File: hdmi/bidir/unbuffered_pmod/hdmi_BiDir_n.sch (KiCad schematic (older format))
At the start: 32 parts

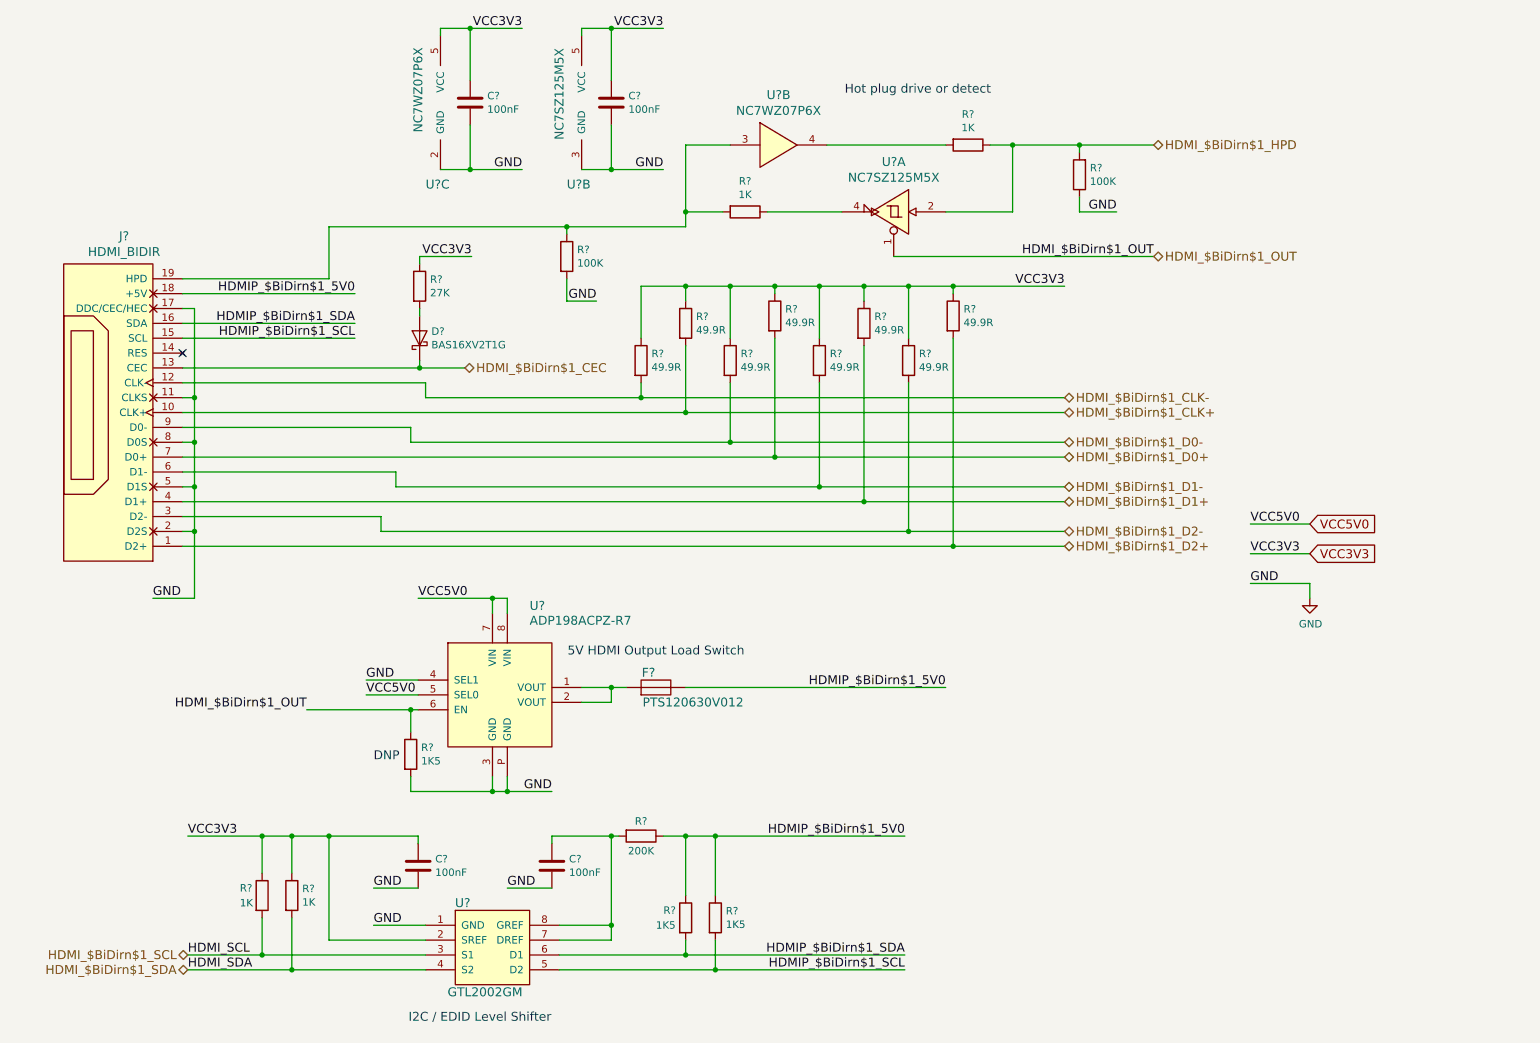
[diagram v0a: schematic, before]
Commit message: Add PMOD Conector and DC/DC Converter
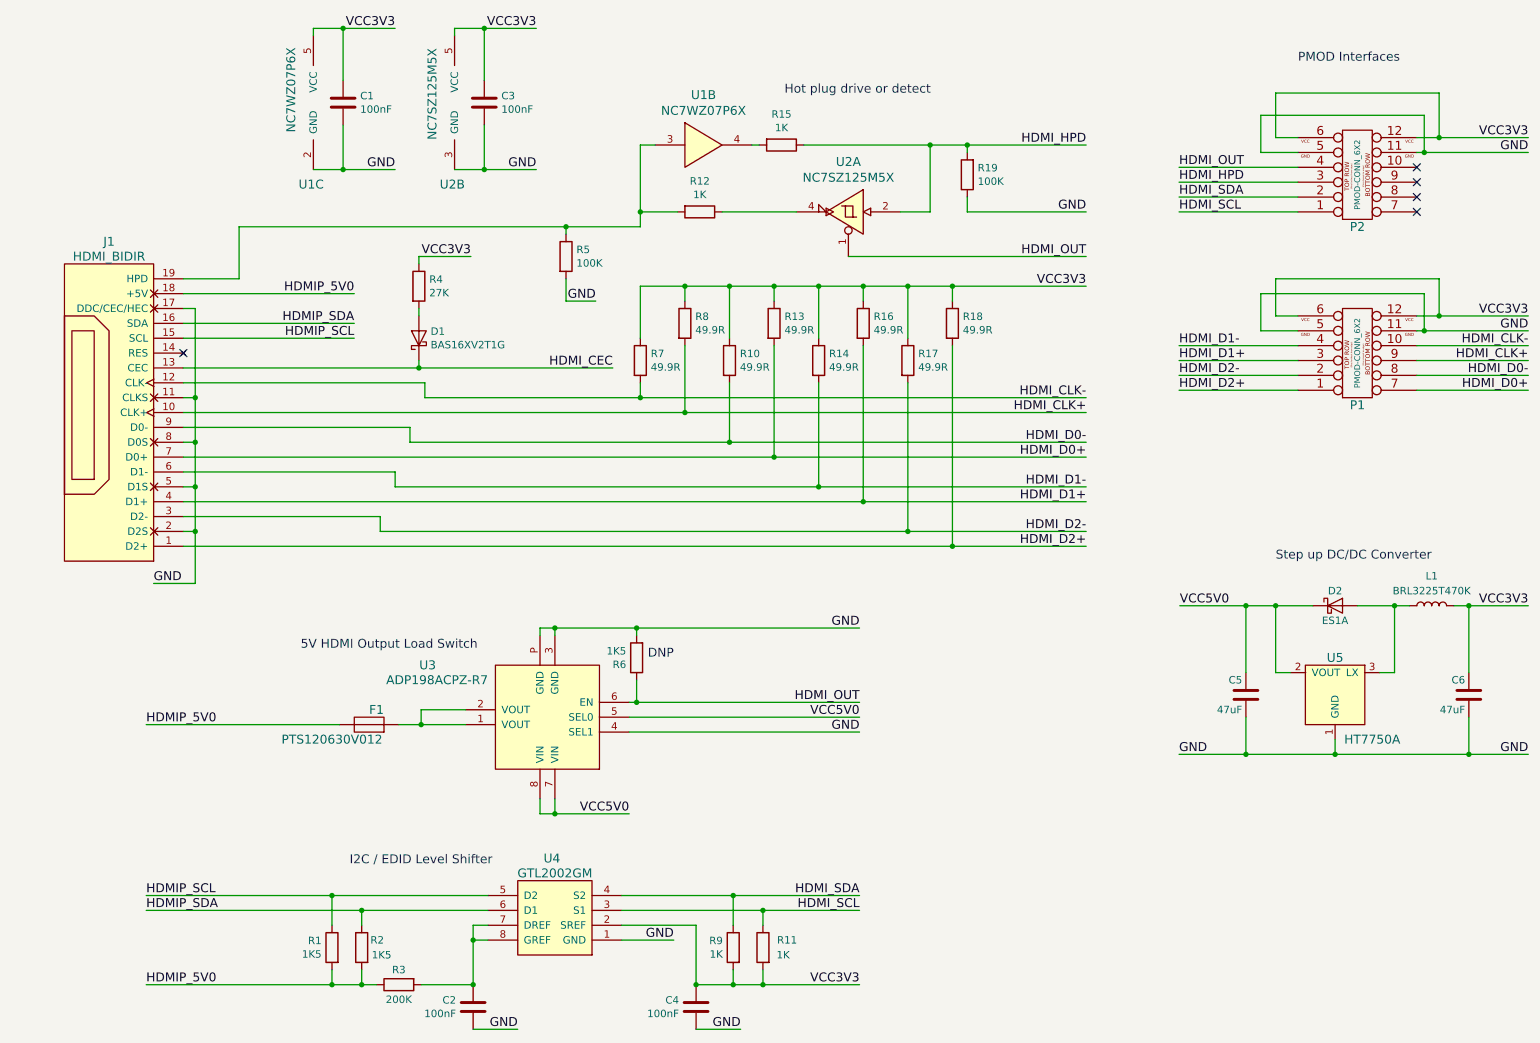
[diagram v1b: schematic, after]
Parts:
- added C5, C6: 47uF, symbol C
- added D2: ES1A, Diodes_SMD:D_SMA_Standard, symbol D_Schottky
- added L1: BRL3225T470K, SMD_Packages:SMD-1210_Pol, symbol L
- added P1, P2: PMOD-CONN_6X2, pmod_pin_array_6x2:pmod_pin_array_6x2, symbol PMOD-CONN_6X2
- added U5: HT7750A, TO_SOT_Packages_SMD:SOT-23, symbol HT7750A
- D1: renamed from D?; footprint (none) -> Diodes_SMD:D_SOD-523
- F1: renamed from F?; footprint (none) -> SMD_Packages:SMD-1206_Pol
- J1: renamed from J?; footprint (none) -> hdmi:HDMI_TH
- U1: renamed from U?; footprint (none) -> TO_SOT_Packages_SMD:SOT-363_SC-70-6
- U2: renamed from U?; footprint (none) -> TO_SOT_Packages_SMD:SOT-23-5
- gave numbers to parts that had none: 25
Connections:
- net GND: now also C5.2, C6.2, P1.11 (P11), P1.5 (P5), P2.11 (P11), P2.5 (P5), U5.1 (GND)
- net VCC3V3: now also R11.2, R9.2, C6.1, L1.2, P1.12 (P12), P1.6 (P6), P2.12 (P12), P2.6 (P6); no longer R11.1, R9.1
- net VCC5V0: now also C5.1, D2.1 (K), U5.2 (VOUT)
- net HDMIP_$BiDirn$1_5V0 renamed HDMIP_5V0
- net HDMIP_5V0: now also R1.2, R2.2; no longer R1.1, R2.1
- net HDMIP_$BiDirn$1_SCL renamed HDMIP_SCL
- net HDMIP_SCL: now also R1.1; no longer R1.2
- net HDMIP_$BiDirn$1_SDA renamed HDMIP_SDA
- net HDMIP_SDA: now also R2.1; no longer R2.2
- net HDMI_$BiDirn$1_CEC renamed HDMI_CEC
- net HDMI_$BiDirn$1_CLK+ renamed HDMI_CLK+
- net HDMI_CLK+: now also P1.9 (P9)
- net HDMI_$BiDirn$1_CLK- renamed HDMI_CLK-
- net HDMI_CLK-: now also P1.10 (P10)
- net HDMI_$BiDirn$1_D0+ renamed HDMI_D0+
- net HDMI_D0+: now also P1.7 (P7)
- net HDMI_$BiDirn$1_D0- renamed HDMI_D0-
- net HDMI_D0-: now also P1.8 (P8)
- net HDMI_$BiDirn$1_D1+ renamed HDMI_D1+
- net HDMI_D1+: now also P1.3 (P3)
- net HDMI_$BiDirn$1_D1- renamed HDMI_D1-
- net HDMI_D1-: now also P1.4 (P4)
- net HDMI_$BiDirn$1_D2+ renamed HDMI_D2+
- net HDMI_D2+: now also P1.1 (P1)
- net HDMI_$BiDirn$1_D2- renamed HDMI_D2-
- net HDMI_D2-: now also P1.2 (P2)
- net HDMI_$BiDirn$1_HPD renamed HDMI_HPD
- net HDMI_HPD: now also P2.3 (P3)
- net HDMI_$BiDirn$1_OUT renamed HDMI_OUT
- net HDMI_OUT: now also P2.4 (P4)
- net HDMI_$BiDirn$1_SCL renamed HDMI_SCL
- net HDMI_SCL: now also R11.1, P2.1 (P1); no longer R11.2
- net HDMI_$BiDirn$1_SDA renamed HDMI_SDA
- net HDMI_SDA: now also R9.1, P2.2 (P2); no longer R9.2
- new net: D2.2 (A), L1.1, U5.3 (LX)
- no-connect marks 1 -> 5
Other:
- note added: "PMOD Interfaces"
- note added: "Step up DC/DC Converter"
- moved on the sheet: C1, C2, C3, C4, F1, R1, R11, R12, R13, R15, R18, R19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
